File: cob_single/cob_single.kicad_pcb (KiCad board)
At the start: 2 copper layers, 50 x 50 mm, 30 parts, among them J1 Conn_01x03, J2 Conn_01x03, Q1 NPN, Q2 NPN, Q3 NPN, U1 MOSFET, U2 MOSFET, U3 MOSFET, U4 WS2811, U5 Inverter

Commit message: Revision 1.0 with linear driver
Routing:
- net G_LED: track 18.0 -> 19.5 mm
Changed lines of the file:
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@@
     (thickness 1.6)
     (drawings 27)
-    (tracks 298)
+    (tracks 299)
     (zones 0)
     (modules 30)
@@
   )
   (setup
-    (last_trace_width 1)
+    (last_trace_width 0.25)
     (user_trace_width 0.5)
     (user_trace_width 0.75)
@@
       (psnegative false)
       (psa4output false)
-      (plotreference true)
-      (plotvalue true)
+      (plotreference false)
+      (plotvalue false)
       (plotinvisibletext false)
       (padsonsilk false)
@@
       (outputformat 1)
       (mirror false)
-      (drillshape 1)
+      (drillshape 0)
       (scaleselection 1)
-      (outputdirectory ""))
+      (outputdirectory "gerber"))
   )
   (net 0 "")
@@
   (segment (start 158.672006 89.42501) (end 164.246996 95) (width 1) (layer F.Cu) (net 5))
   (segment (start 166.23 95) (end 168.78 95) (width 1) (layer F.Cu) (net 5))
+  (segment (start 153.5 86.8875) (end 153.5 88.4375) (width 0.25) (layer F.Cu) (net 5))
   (segment (start 153.5 95.8875) (end 153.5 97.4375) (width 0.25) (layer F.Cu) (net 6))
   (segment (start 166.23 96.7) (end 168.78 96.7) (width 1) (layer F.Cu) (net 6))

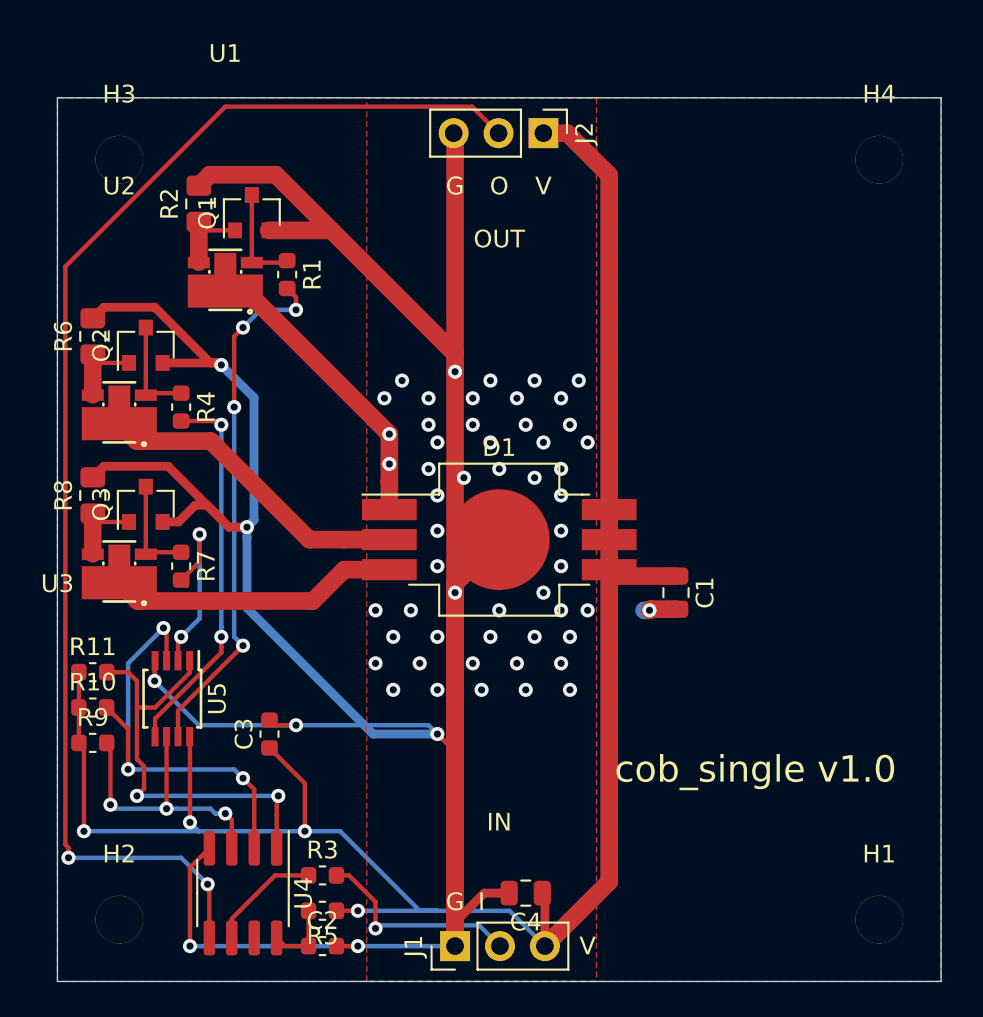
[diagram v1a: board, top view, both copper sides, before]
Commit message: Re-do revision 1.0 with 5V switching driver
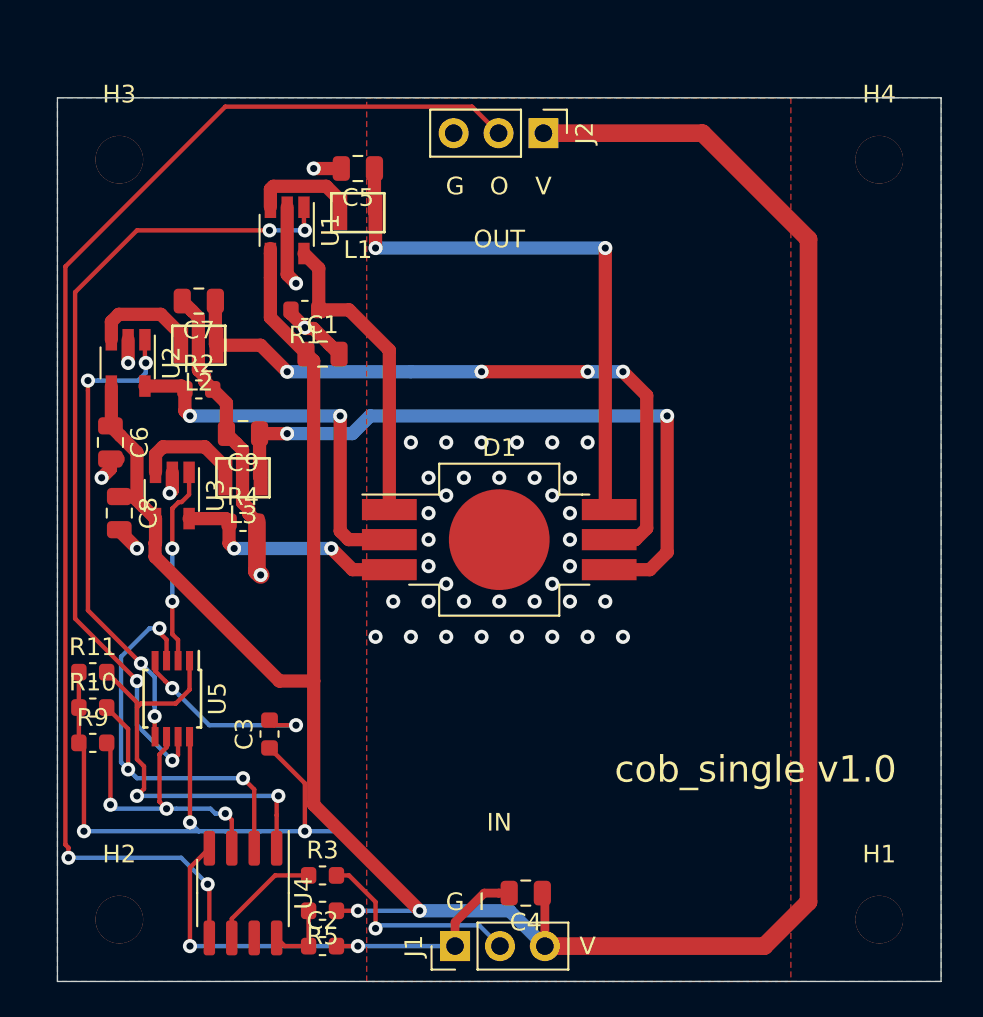
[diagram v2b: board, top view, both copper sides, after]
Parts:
- removed Q1, Q2, Q3: NPN, Package_TO_SOT_SMD:SOT-23
- removed R6, R8: .36, Resistor_SMD:R_0805_2012Metric_Pad1.15x1.40mm_HandSolder
- removed R7: 100, Resistor_SMD:R_0603_1608Metric
- added C5: 10uF, Capacitor_SMD:C_0805_2012Metric, F.Cu at (167.0, 74.0)
- added C6: 10uF, Capacitor_SMD:C_0805_2012Metric, F.Cu at (153.0, 89.5)
- added C7: 10uF, Capacitor_SMD:C_0805_2012Metric, F.Cu at (158.0, 81.5)
- added C8: 10uF, Capacitor_SMD:C_0805_2012Metric, F.Cu at (153.5, 93.5)
- added C9: 10uF, Capacitor_SMD:C_0805_2012Metric, F.Cu at (160.5, 89.0)
- added L1: 4.7uH, homebrew:1008_(2520_METRIC), F.Cu at (167.0, 76.5)
- added L2: 4.7uH, homebrew:1008_(2520_METRIC), F.Cu at (158.0, 84.0)
- added L3: 4.7uH, homebrew:1008_(2520_METRIC), F.Cu at (160.5, 91.5)
- R1, R4: value 100 -> .143
- R2: value .36 -> .143; footprint Resistor_SMD:R_0805_2012Metric_Pad1.15x1.40mm_HandSolder -> Resistor_SMD:R_0603_1608Metric
- U1, U2, U3: value MOSFET -> PAM2804_LED_DRIVER; footprint homebrew:6-TSOP-MOSFET-SI3424CDV-T1-GE3 -> Package_TO_SOT_SMD:TSOT-23-5
- U5: value Inverter -> 3_Inverter_TC7WH14FU,LJ(CT
- moved C1 24.1 mm to (165.0, 84.5), turned to 0 degrees
- moved R2 10.5 mm to (158.0, 86.5), turned to 0 degrees
- moved R4 7.38 mm to (160.5, 94.0), turned to 0 degrees
- moved U3 5.00 mm to (156.5, 92.5), turned to 270 degrees
- moved U1 4.30 mm to (163.0, 77.5), turned to 270 degrees
- moved U2 2.55 mm to (154.0, 85.0), turned to 270 degrees
- moved R1 2.24 mm to (164.0, 82.0), turned to 180 degrees
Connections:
- D1 pad 1: R_LED -> R_LED_CATHODE
- D1 pad 2: G_LED -> G_LED_CATHODE
- D1 pad 3: B_LED -> B_LED_CATHODE
- D1 pad 4: VCC -> B_LED_ANODE
- D1 pad 5: VCC -> G_LED_ANODE
- D1 pad 6: VCC -> R_LED_ANODE
- R1 pad 1: Net-(Q1-Pad3) -> R_LED_CATHODE
- R1 pad 2: R_SIGNAL -> GND
- R2 pad 1: Net-(Q1-Pad1) -> G_LED_CATHODE
- R4 pad 1: Net-(Q2-Pad3) -> B_LED_CATHODE
- R4 pad 2: G_SIGNAL -> GND
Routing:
- net GND: track 198.1 -> 72.1 mm, vias 59 -> 48
- net VCC: track 111.5 -> 193.9 mm, vias 4 -> 5
- net G_LED_ANODE: track 0.00 -> 38.0 mm, vias 0 -> 4
- net B_LED_ANODE: track 0.00 -> 37.4 mm, vias 0 -> 2
- net R_LED_ANODE: track 0.00 -> 32.4 mm, vias 0 -> 2
- net G_LED_CATHODE: track 0.00 -> 22.0 mm, vias 0 -> 2
- net G_LED: track 19.5 -> 0.00 mm
- net R_LED: track 18.5 -> 0.00 mm, vias 2 -> 0
- net B_LED: track 18.0 -> 0.00 mm
- net R_LED_CATHODE: track 0.00 -> 17.5 mm
- net R_SIGNAL: track 29.9 -> 46.0 mm
- net B_LED_CATHODE: track 0.00 -> 13.2 mm, vias 0 -> 2
- net Net-(L3-Pad1): track 0.00 -> 6.22 mm
- net Net-(L2-Pad1): track 0.00 -> 6.22 mm
- net Net-(L1-Pad1): track 0.00 -> 6.07 mm
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
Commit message: Convert v1.0 to 12v supply/12v tolerant switching driver.
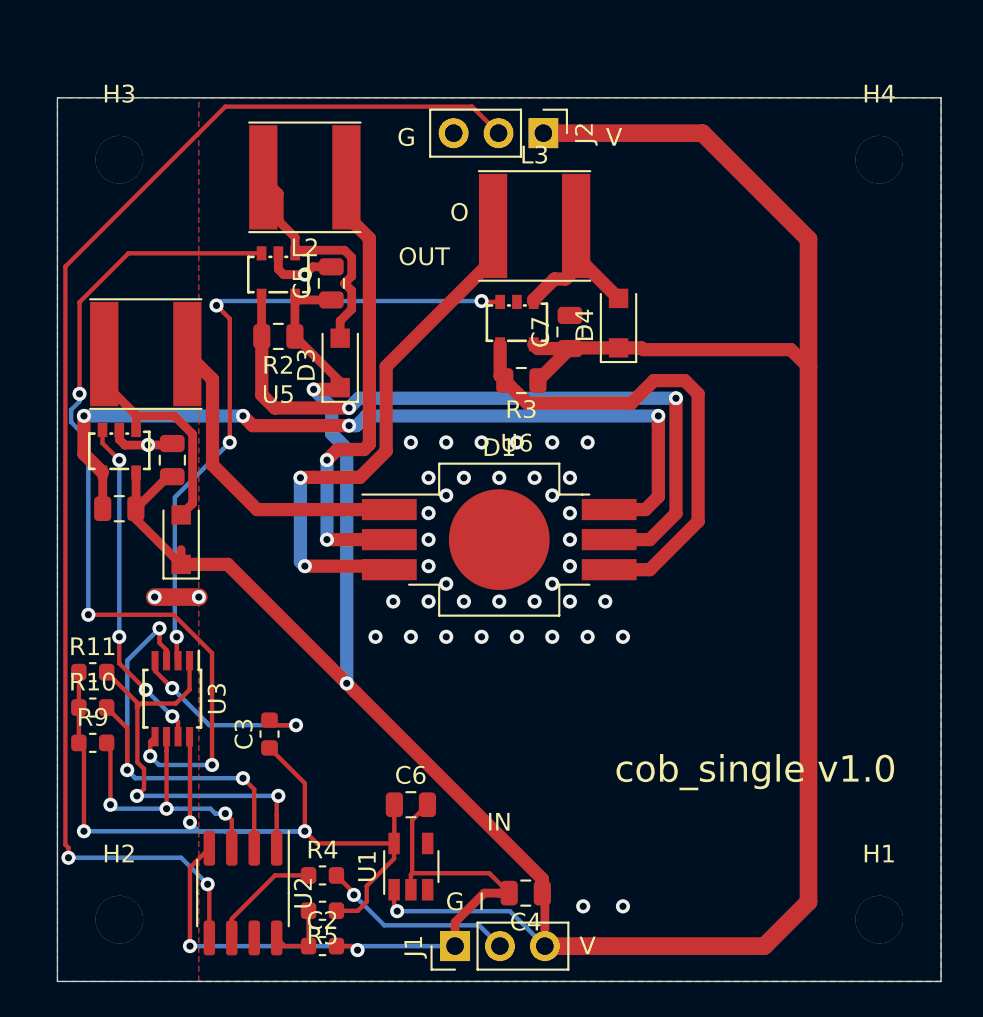
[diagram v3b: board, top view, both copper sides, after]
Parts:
- removed C8, C9: 10uF, Capacitor_SMD:C_0805_2012Metric
- removed the R4 at (160.5, 94.0)
- removed the U2 at (154.0, 85.0)
- added D2: D_Schottky, Diode_SMD:D_SOD-123F, F.Cu at (157.0, 95.0)
- added D3: D_Schottky, Diode_SMD:D_SOD-123F, F.Cu at (166.0, 85.0)
- added D4: D_Schottky, Diode_SMD:D_SOD-123F, F.Cu at (181.8, 82.8)
- added R3: .143, Resistor_SMD:R_0805_2012Metric, F.Cu at (176.2, 86.0)
- added U4: AL8860, homebrew:SOT-25, F.Cu at (153.5, 90.0)
- added U6: AL8860, homebrew:SOT-25, F.Cu at (176.0, 82.8)
- L1, L2, L3: value 4.7uH -> 47uH; footprint homebrew:1008_(2520_METRIC) -> Inductor_SMD:L_Taiyo-Yuden_NR-60xx
- R1, R2: footprint Resistor_SMD:R_0603_1608Metric -> Resistor_SMD:R_0805_2012Metric
- U1: value PAM2804_LED_DRIVER -> AP7370
- U3: value PAM2804_LED_DRIVER -> INVERTER; footprint Package_TO_SOT_SMD:TSOT-23-5 -> Package_SO:TSSOP-8_3x3mm_P0.65mm
- U5: value 3_Inverter_TC7WH14FU,LJ(CT -> AL8860; footprint Package_SO:TSSOP-8_3x3mm_P0.65mm -> homebrew:SOT-25
- moved U1 36.7 mm to (170.0, 113.5), turned to 90 degrees
- moved C6 26.6 mm to (170.0, 110.0), turned to 0 degrees
- moved U5 24.7 mm to (162.5, 80.0), turned to 0 degrees
- moved L3 21.8 mm to (177.0, 77.2)
- moved C7 21.1 mm to (179.0, 83.2), turned to 90 degrees
- moved R1 15.4 mm to (153.5, 93.2)
- moved L1 14.4 mm to (155.0, 84.5), turned to 180 degrees
- moved U3 11.5 mm to (156.5, 104.0)
- moved L2 11.2 mm to (164.0, 74.5), turned to 180 degrees
- moved C1 10.4 mm to (156.5, 90.5), turned to 90 degrees
- moved C5 6.67 mm to (165.5, 80.5), turned to 90 degrees
- moved R2 5.41 mm to (162.5, 83.5), turned to 180 degrees
- renumbered R3 to R4, U4 to U2
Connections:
- C1 pad 1: VCC -> +12V
- C3 pad 1: VCC -> +5V
- C4 pad 1: VCC -> +12V
- C5 pad 1: R_LED_ANODE -> +12V
- C6 pad 1: VCC -> +5V
- C7 pad 1: G_LED_ANODE -> +12V
- D1 pad 1: R_LED_CATHODE -> R_LED_K
- D1 pad 2: G_LED_CATHODE -> G_LED_K
- D1 pad 3: B_LED_CATHODE -> B_LED_K
- D1 pad 4: B_LED_ANODE -> B_LED_A
- D1 pad 5: G_LED_ANODE -> G_LED_A
- D1 pad 6: R_LED_ANODE -> R_LED_A
- J1 pad 3: VCC -> +12V
- J2 pad 1: VCC -> +12V
- L1 pad 1: Net-(L1-Pad1) -> R_LED_K
- L1 pad 2: R_LED_ANODE -> Net-(D2-Pad2)
- L2 pad 1: Net-(L2-Pad1) -> G_LED_K
- L2 pad 2: G_LED_ANODE -> Net-(D3-Pad2)
- L3 pad 1: Net-(L3-Pad1) -> B_LED_K
- L3 pad 2: B_LED_ANODE -> Net-(D4-Pad2)
- R1 pad 1: R_LED_CATHODE -> +12V
- R1 pad 2: GND -> R_LED_A
- R10 pad 1: VCC -> +5V
- R11 pad 1: VCC -> +5V
- R2 pad 1: G_LED_CATHODE -> +12V
- R2 pad 2: GND -> G_LED_A
- R5 pad 1: VCC -> +5V
- R9 pad 1: VCC -> +5V
- U1 pad 1: R_SIGNAL -> +12V
- U1 pad 3: Net-(L1-Pad1) -> (no net)
- U1 pad 4: VCC -> (no net)
- U1 pad 5: R_LED_CATHODE -> +5V
- U3 pad 1: B_SIGNAL -> R_INVERTED
- U3 pad 2: GND -> B_SIGNAL
- U3 pad 3: Net-(L3-Pad1) -> G_INVERTED
- U3 pad 4: VCC -> GND
- U3 pad 5: B_LED_CATHODE -> G_SIGNAL
- U5 pad 1: R_INVERTED -> Net-(D3-Pad2)
- U5 pad 2: B_SIGNAL -> GND
- U5 pad 3: G_INVERTED -> G_SIGNAL
- U5 pad 4: GND -> G_LED_A
- U5 pad 5: G_SIGNAL -> +12V
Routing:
- net VCC: track 193.9 -> 0.00 mm, vias 5 -> 0
- net +12V: track 0.00 -> 169.0 mm, vias 0 -> 3
- net +5V: track 0.00 -> 53.1 mm, vias 0 -> 3
- net R_LED_A: track 0.00 -> 46.3 mm, vias 0 -> 4
- net G_LED_A: track 0.00 -> 40.5 mm, vias 0 -> 2
- net G_LED_ANODE: track 38.0 -> 0.00 mm, vias 4 -> 0
- net B_LED_ANODE: track 37.4 -> 0.00 mm, vias 2 -> 0
- net R_LED_ANODE: track 32.4 -> 0.00 mm, vias 2 -> 0
- net B_LED_K: track 0.00 -> 30.9 mm, vias 0 -> 2
- net B_LED_A: track 0.00 -> 27.8 mm
- net R_SIGNAL: track 46.0 -> 19.1 mm
- net B_SIGNAL: track 11.3 -> 37.9 mm, vias 2 -> 4
- net G_LED_K: track 0.00 -> 26.4 mm, vias 0 -> 2
- net G_LED_CATHODE: track 22.0 -> 0.00 mm, vias 2 -> 0
- net G_SIGNAL: track 27.1 -> 48.9 mm
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
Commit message: High-power revision 1.1:
- Fixed LED thermal pad to not connect to ground
- Fixed clearance for LED lens
- Added orientation for diodes and LED
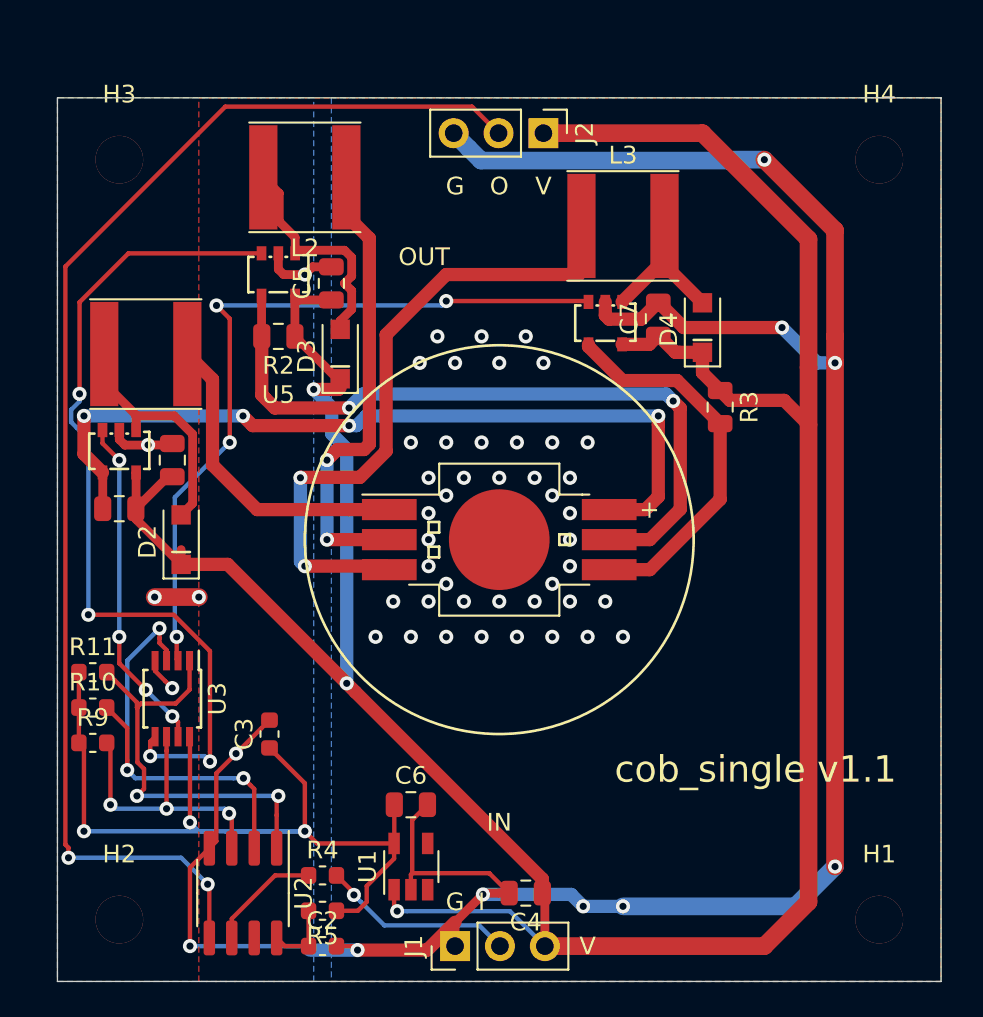
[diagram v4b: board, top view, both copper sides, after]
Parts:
- D1: value LED_RGB -> LED_RGB_EP; footprint LED_SMD:LED_RGB_Getian_GT-P6PRGB4303 -> homebrew:LED_RGB_EPISTAR_6PIN_RGB
- D2, D3, D4: footprint Diode_SMD:D_SOD-123F -> homebrew:D_SOD-123F
- U1: value AP7370 -> 5V_REG_AP7370-50W5-7
- U3: value INVERTER -> 3_Inverter_TC7WH14FU,LJ(CT
- U4, U5, U6: value AL8860 -> AL8860_LED_DRIVER
- moved R3 11.3 mm to (187.5, 87.5), turned to 270 degrees
- moved C7 5.06 mm to (184.0, 82.5)
- moved L3 5.00 mm to (182.0, 77.2)
- moved U6 5.00 mm to (181.0, 82.8)
- moved D4 4.76 mm to (186.5, 83.0)
- moved D3 0.50 mm to (166.0, 84.5)
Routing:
- net GND: track 61.0 -> 160.6 mm, vias 46 -> 15
- net B_LED_A: track 27.8 -> 21.6 mm
- net B_LED_K: track 30.9 -> 37.2 mm
- net +12V: track 169.0 -> 163.9 mm
- net B_SIGNAL: track 37.9 -> 42.9 mm
- net Net-(D4-Pad2): track 11.3 -> 10.5 mm
- net Net-(D3-Pad2): track 13.7 -> 13.2 mm
- net Net-(D1-Pad7): vias 0 -> 43
- added copper zone on B.Cu, net Net-(D1-Pad7)
- added copper zone on F.Cu, net Net-(D1-Pad7)
- removed copper zone on F.Cu, net GND
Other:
- board text added: "cob_single v1.1"
- board text removed: "cob_single v1.0"
